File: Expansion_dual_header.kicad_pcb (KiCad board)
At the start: 2 copper layers, 101.6 x 101.6 mm, 30 parts, among them IC1 STM32L051C6T6, J1 Conn_01x05_Pin, J2 Conn_01x03_Pin, J3 ESQ-120-14-G-S, J4 ESQ-120-14-G-S, J5 Conn_01x02_Pin, J6 Conn_01x02_Pin, SW1 PTS 647 SN50 SMTR2 LFS, Y1 8MHz, Y2 32.768KHZ

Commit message: added footprints Servos on PCB
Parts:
- added J10: Conn_01x03_Pin, Connector_PinHeader_2.54mm:PinHeader_1x03_P2.54mm_Vertical, F.Cu at (221.8, 85.4)
- added J11: Conn_01x03_Pin, Connector_PinHeader_2.54mm:PinHeader_1x03_P2.54mm_Vertical, F.Cu at (226.4, 85.4)
- added J12: Conn_01x03_Pin, Connector_PinHeader_2.54mm:PinHeader_1x03_P2.54mm_Vertical, F.Cu at (231.0, 85.4)
- C1, C2: value 10pF -> 10p
- C3, C4: value 20pF -> 15p
- R1: value 390 -> 300
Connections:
- IC1 pad 11: /Microcontroller/PA1 -> /Servos/SERVO1_CTRL
- IC1 pad 21: /Microcontroller/PB10 -> /Servos/SERVO3_CTRL

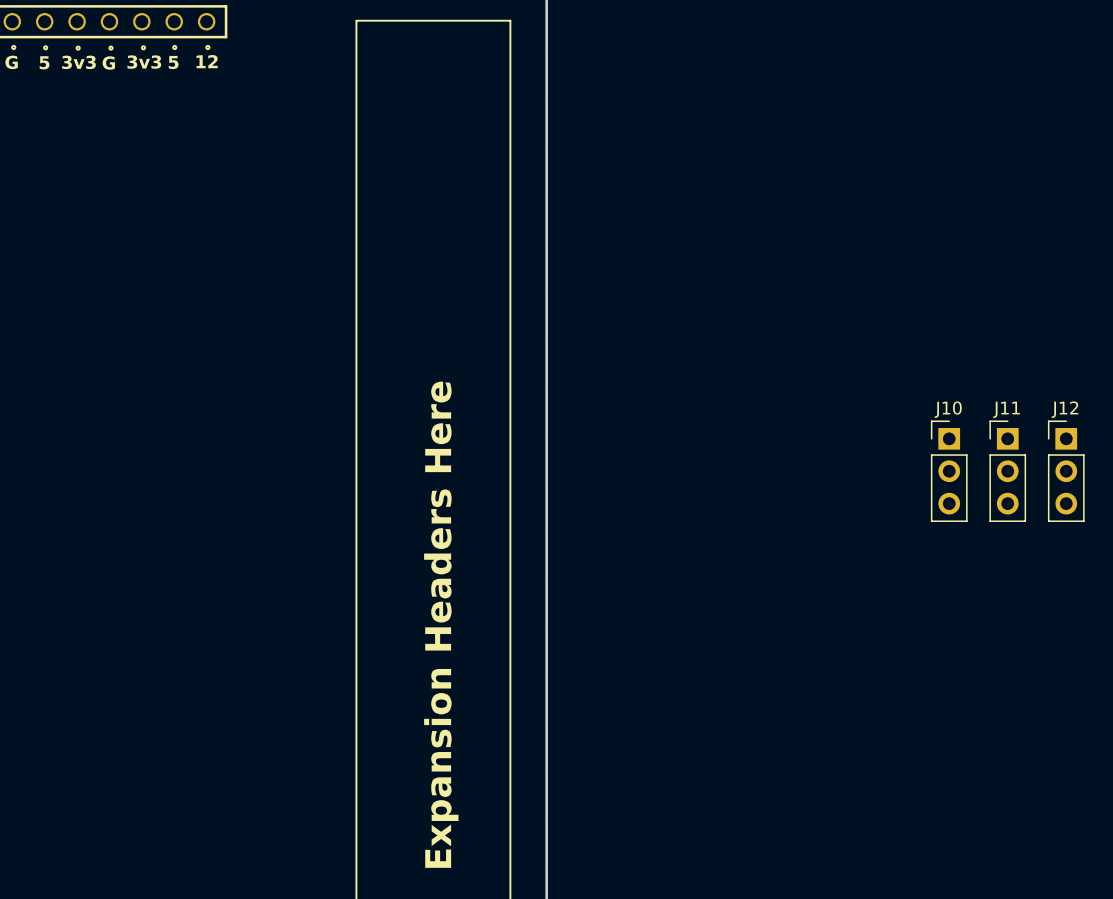
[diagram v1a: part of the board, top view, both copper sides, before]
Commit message: added MOSFET, and switch for Servos
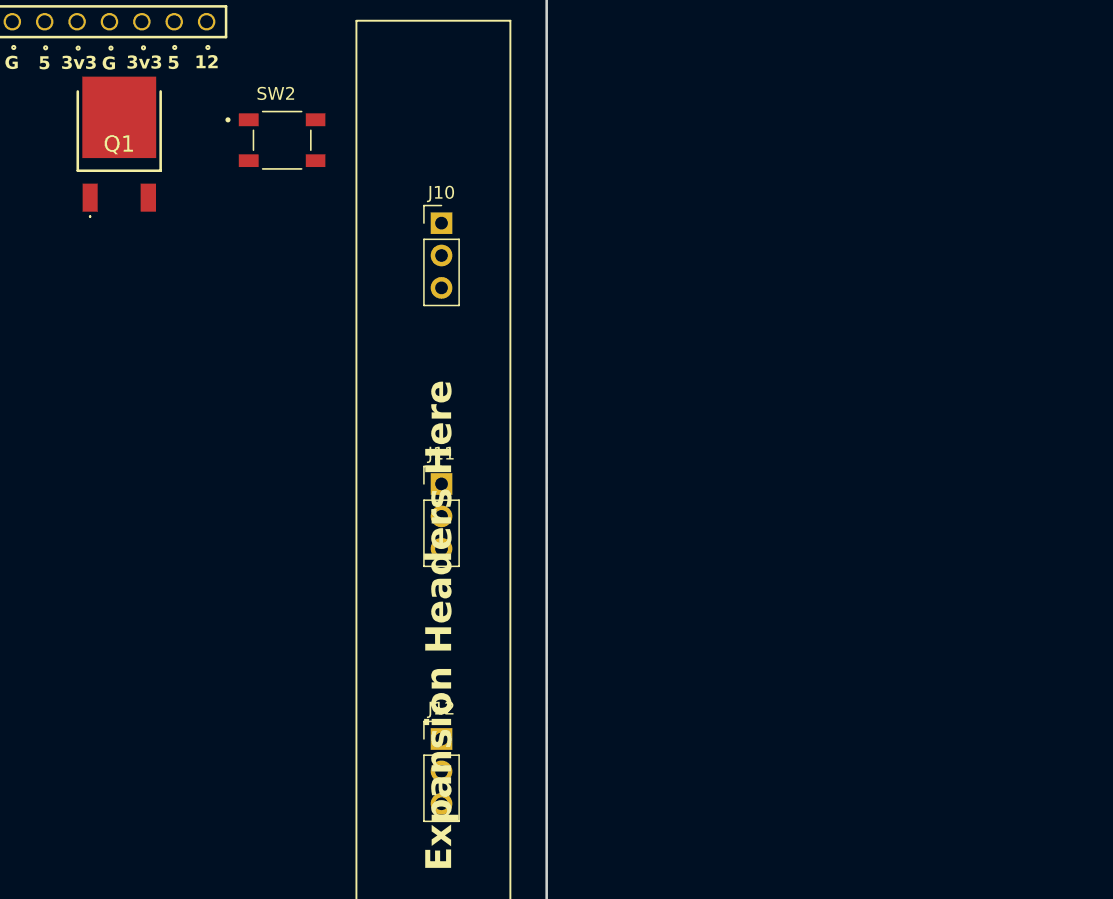
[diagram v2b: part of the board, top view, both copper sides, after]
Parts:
- added Q1: IPD90N04S4-05, AquaPartsLib:IPD90N04S405, F.Cu at (156.7, 62.3)
- added SW2: PTS 647 SN50 SMTR2 LFS, AquaPartsLib:SW_PTS_647_SN50_SMTR2_LFS, F.Cu at (169.5, 62.0)
- moved J12 54.4 mm to (182.0, 109.0)
- moved J11 44.6 mm to (182.0, 89.0)
- moved J10 43.3 mm to (182.0, 68.5)
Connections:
- J10 pad 3: +5V -> 5V_Servos
- J11 pad 3: +5V -> 5V_Servos
- J12 pad 3: +5V -> 5V_Servos

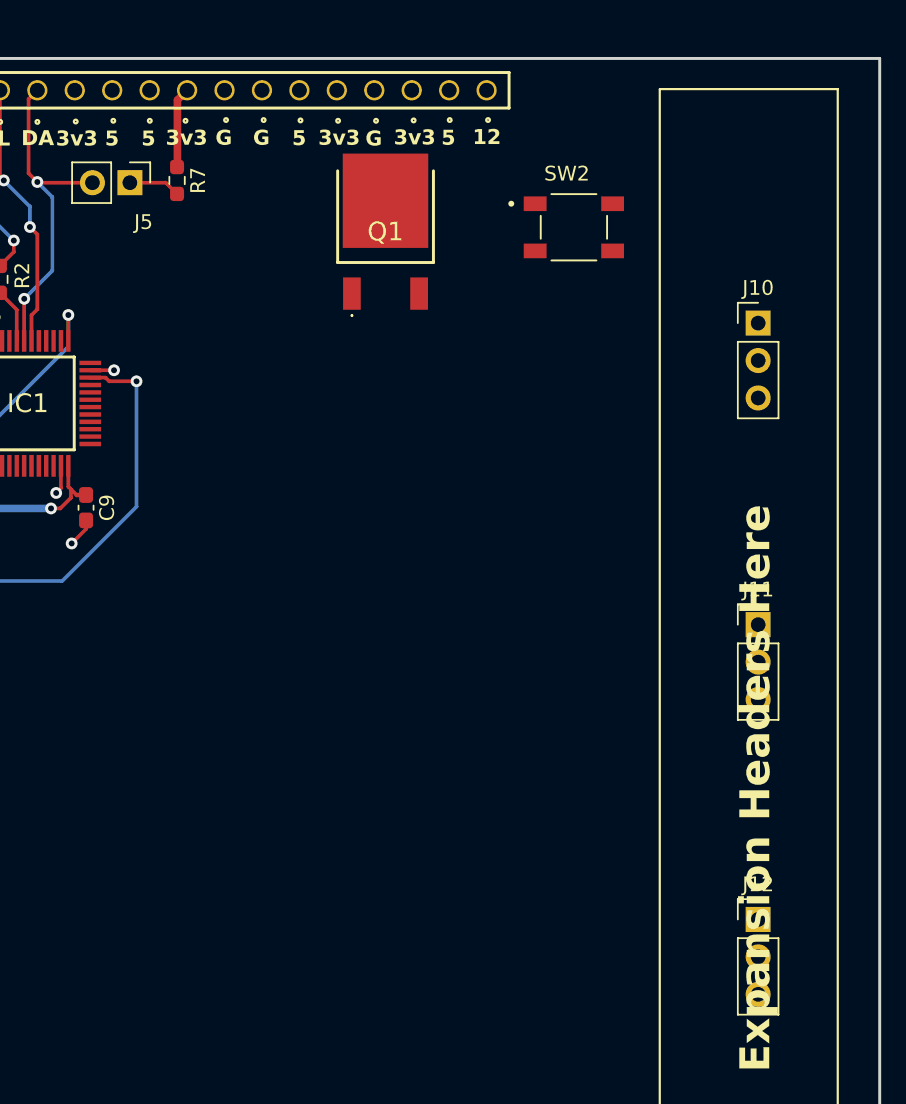
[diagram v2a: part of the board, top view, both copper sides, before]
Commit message: add trace lines to PCB
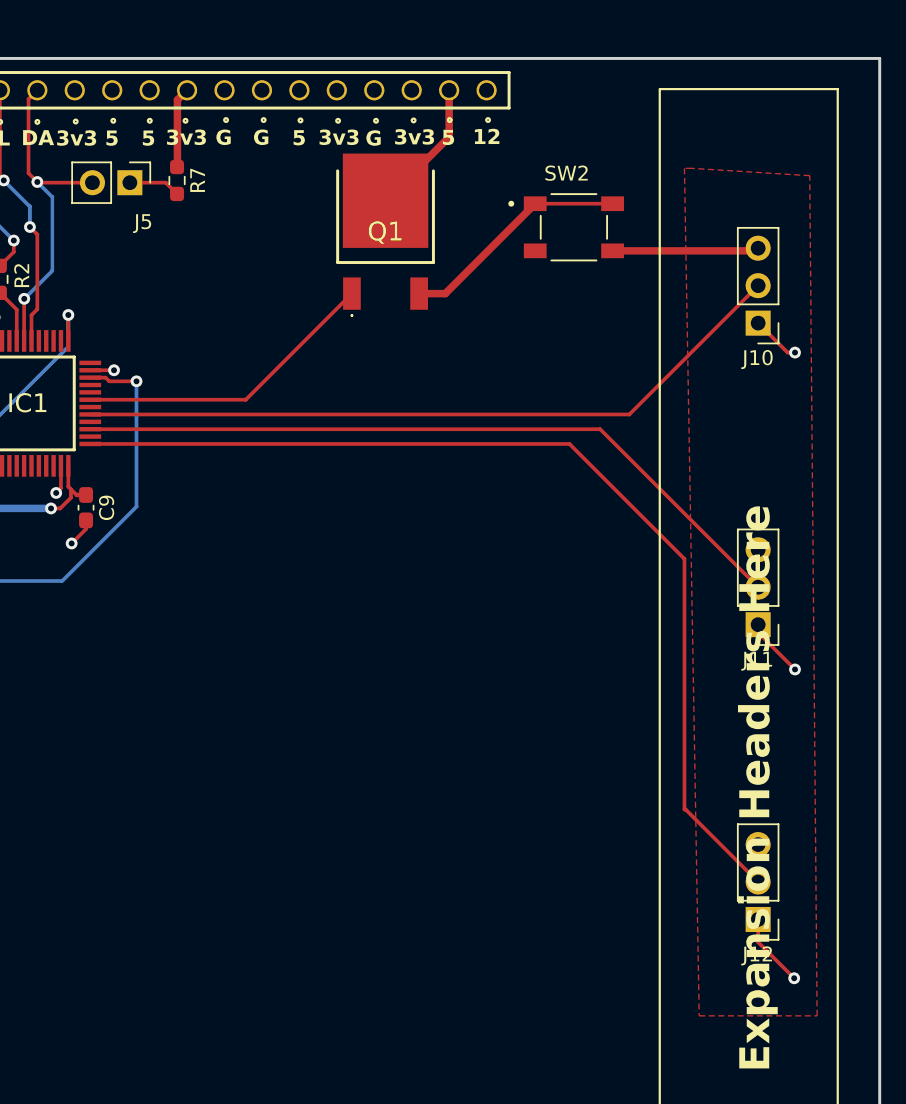
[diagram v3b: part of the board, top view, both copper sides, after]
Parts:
- turned J10 to 180 degrees
- turned J11 to 180 degrees
- turned J12 to 180 degrees
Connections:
- IC1 pad 11: /Servos/SERVO1_CTRL -> /Microcontroller/PA1
- IC1 pad 21: /Servos/SERVO3_CTRL -> /Microcontroller/PB10
- IC1 pad 27: /Microcontroller/PB14 -> /Servos/SERVO3_CTRL
- IC1 pad 29: /Microcontroller/PA8 -> /Servos/SERVO1_CTRL
- J12 pad 2: /Microcontroller/PB1 -> /Microcontroller/PB12
- Q1 pad 1: /Microcontroller/PA8 -> /Microcontroller/PA10
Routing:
- net /Microcontroller/PB12: track 0.00 -> 67.7 mm
- net /Servos/SERVO3_CTRL: track 0.00 -> 49.8 mm
- net /Servos/SERVO1_CTRL: track 0.00 -> 48.9 mm
- net /Microcontroller/PA10: track 0.00 -> 20.7 mm
- net Net-(Q1-S): track 0.00 -> 15.7 mm
- net GND: track 37.2 -> 50.1 mm, vias 17 -> 20
- net 5V_Servos: track 0.00 -> 9.95 mm
- net +5V: track 19.4 -> 28.7 mm
- added copper zone on F.Cu, net 5V_Servos
